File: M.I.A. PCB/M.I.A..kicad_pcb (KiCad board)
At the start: 6 copper layers, 50.8 x 106.6 mm, 160 parts, among them J1 USB_C_Receptacle_USB2.0_16P, J10 Conn_01x03, J11 Conn_01x03, J12 Conn_Coaxial, J13 Screw_Terminal_01x02, J14 Screw_Terminal_01x02, J15 Screw_Terminal_01x02, J16 Screw_Terminal_01x02, J17 Screw_Terminal_01x02, J18 Screw_Terminal_01x02, J2 Conn_01x02_Pin, J3 Conn_01x03, J4 Conn_01x03, J5 Conn_01x03, J6 Conn_01x03, J7 MSD-4-A, J8 Conn_01x03, J9 Conn_01x03, Q1 AO3400A, Q2 AO3400A, Q3 AO3400A, Q4 AO3400A, SW1 SW_Push, SW2 SW_Push, U1 W25Q128JVS, U11 AMS1117-3.3, U11 INA219AxDCN, U12 AP62150WU, U13 TPS2121RUXR, U14 AP62150WU, U15 74AHC541, U16 RFM95W-915S2, U17 TLV70233_SOT23-5, U2 RP2350B-QFN80, U3 MMC5983MA, U4 ICM-45686, U5 MS5611-01BA, U6 TMP117xxDRV, U7 MAX-M10S, U8 KX134-1211, U9 TPS2121RUXR, Y1 ABM8-272-T3

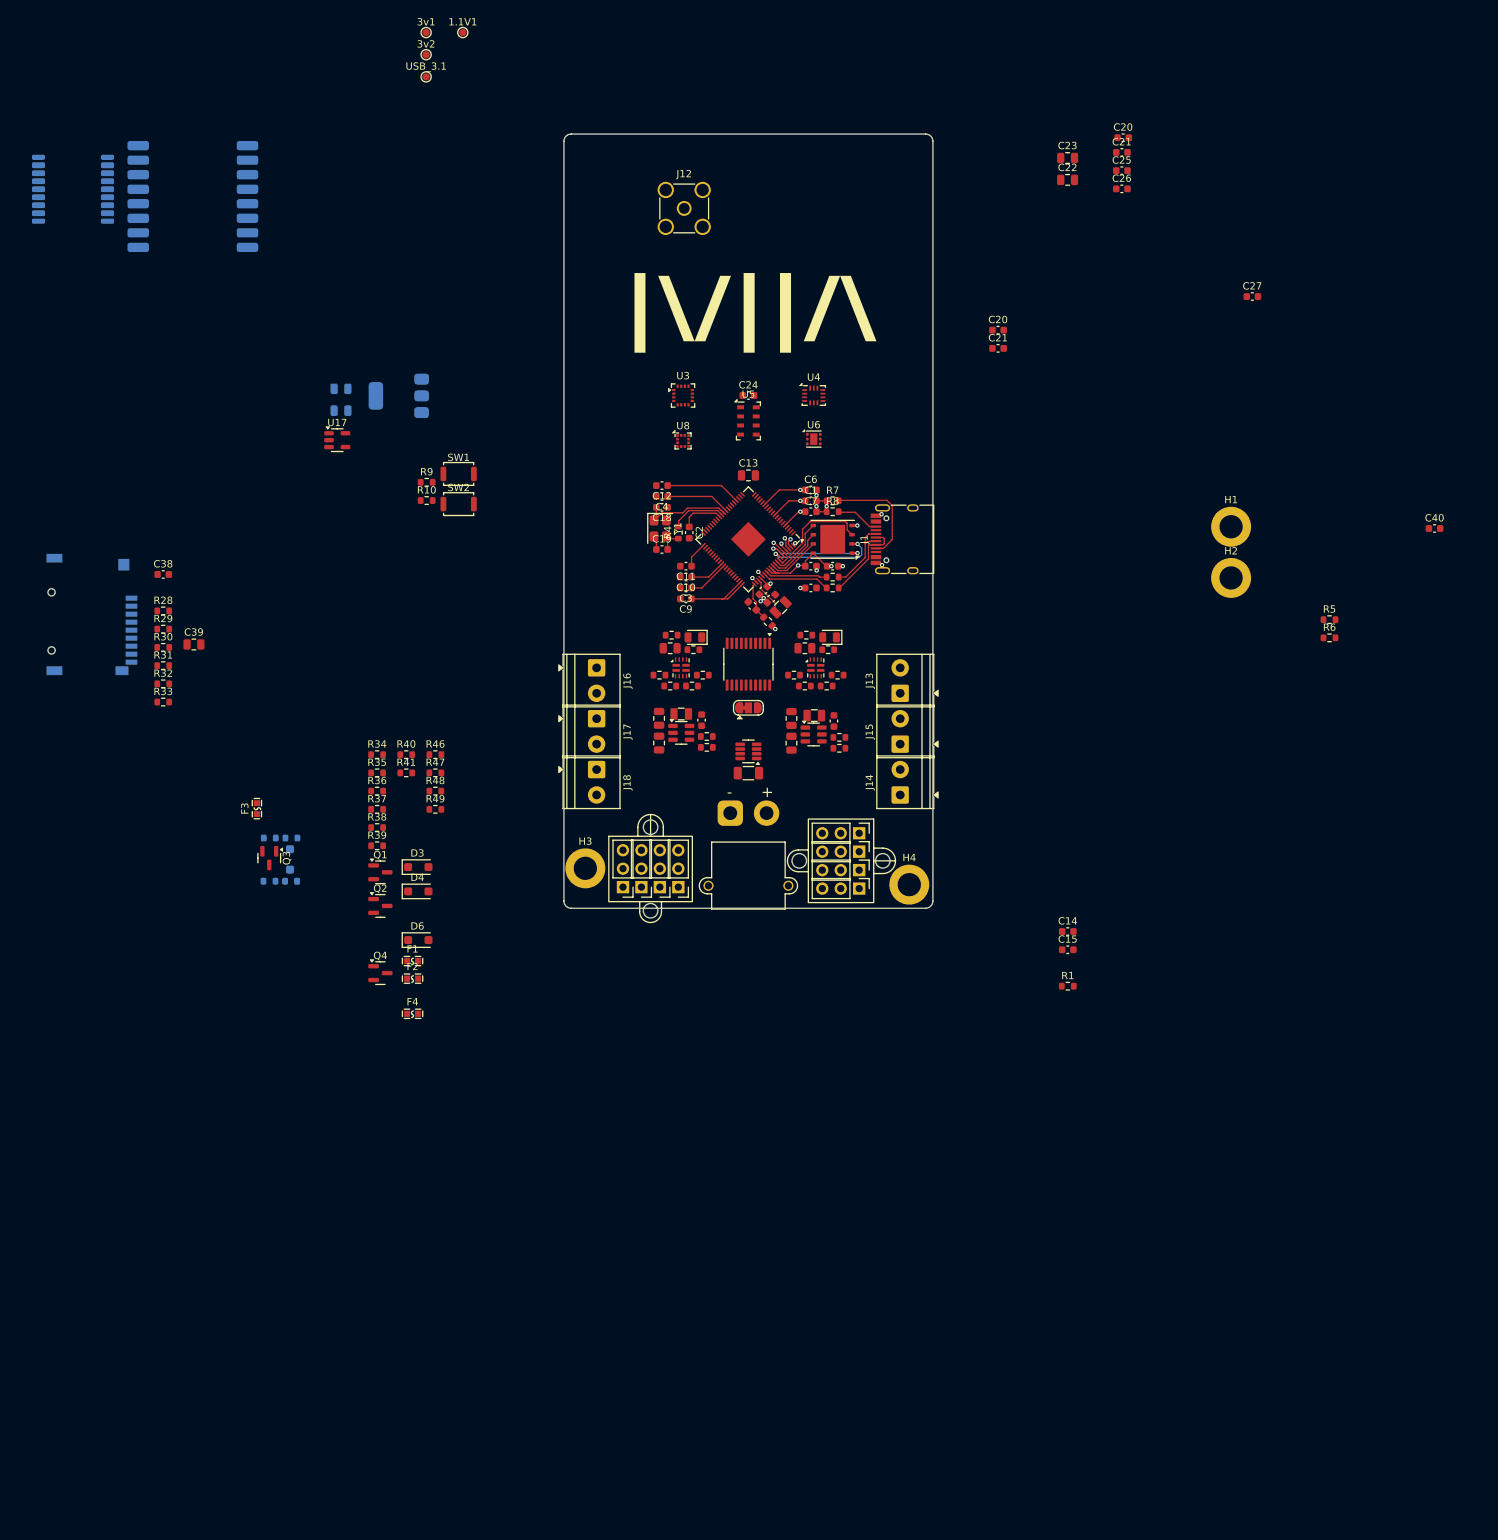
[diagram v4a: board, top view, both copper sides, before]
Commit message: Finished Layout other than gps, extra connectors, and ignition lines
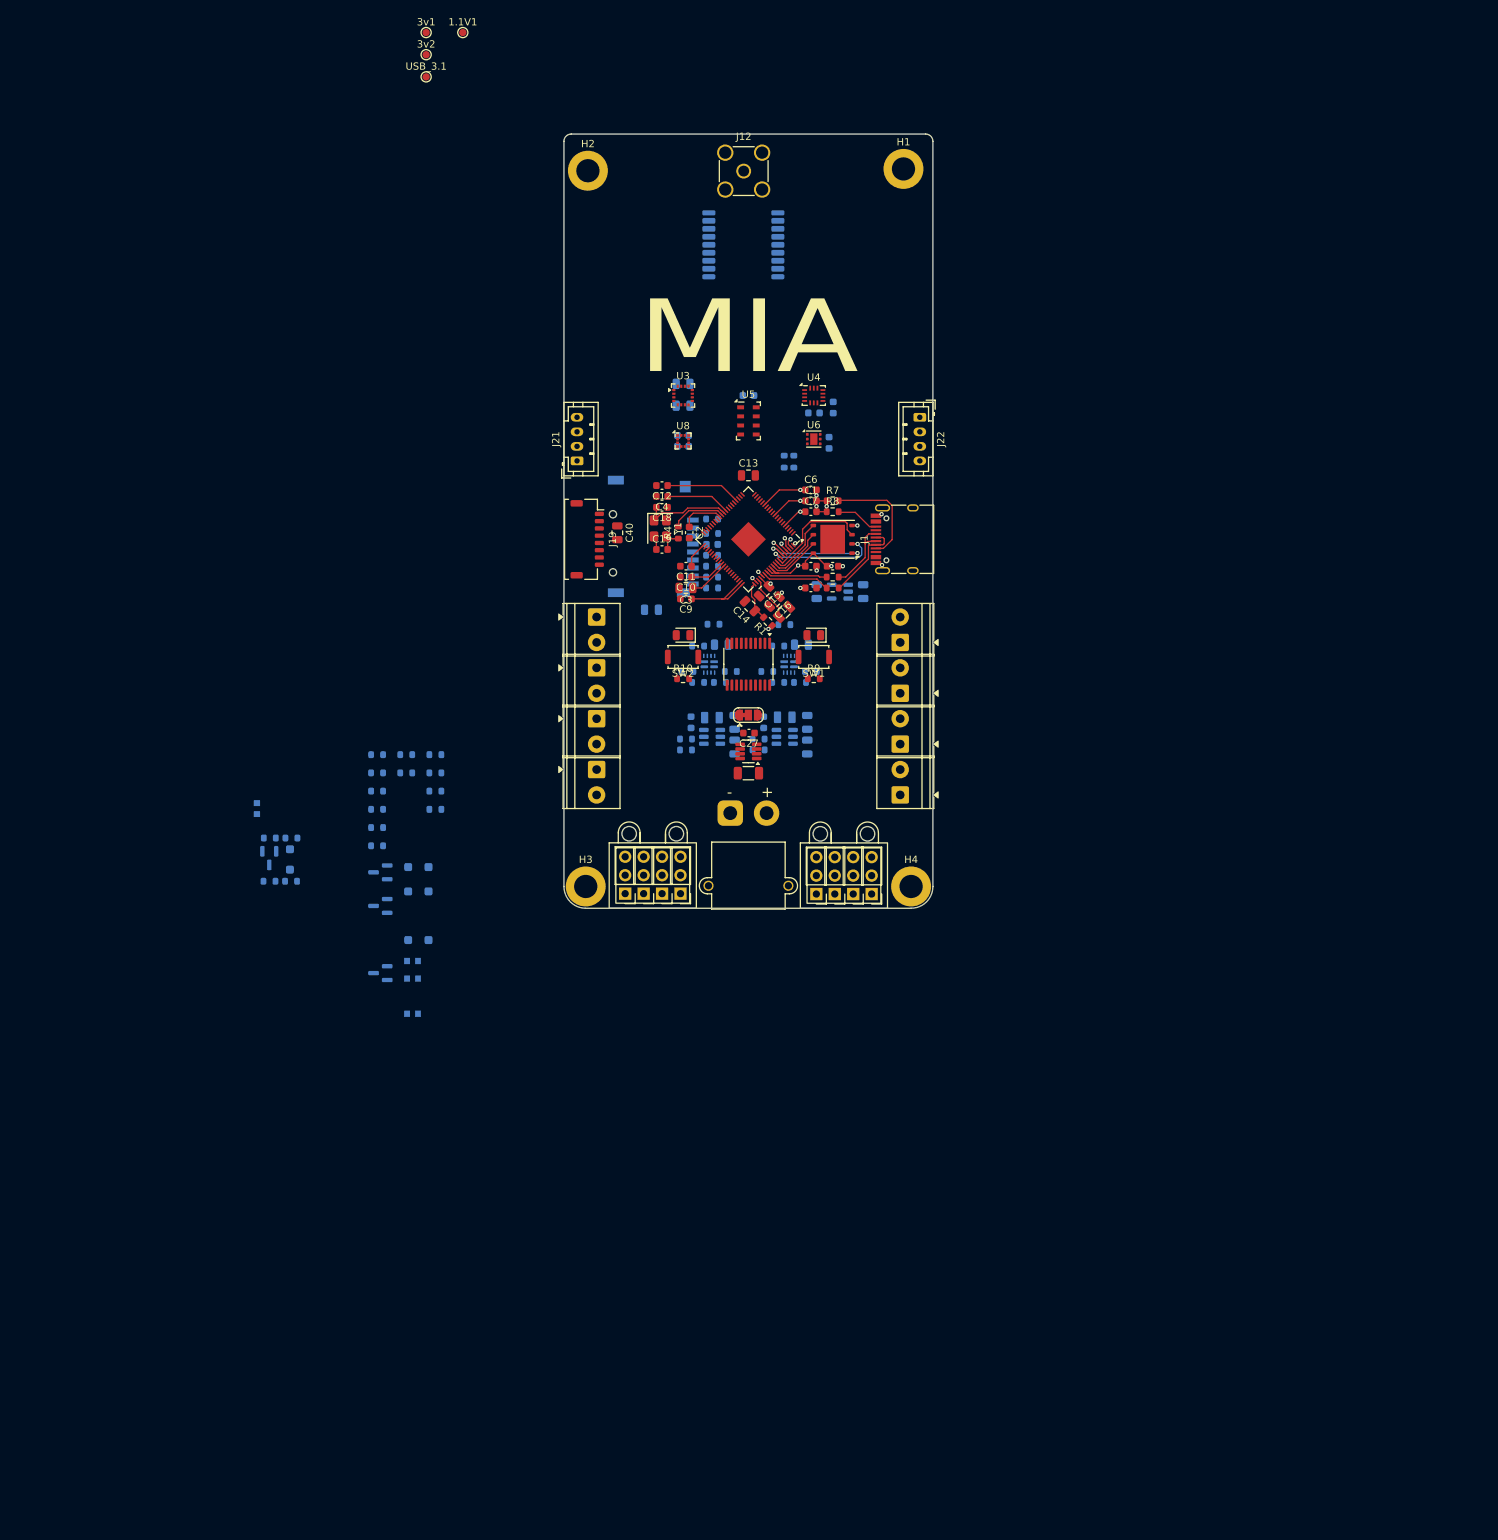
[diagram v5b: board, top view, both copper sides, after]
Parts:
- removed the C14 at (89.4, 124.8)
- removed the C14 at (45.9, 80.0)
- removed the C15 at (89.4, 127.3)
- removed the C15 at (47.5, 77.8)
- removed the C20 at (79.8, 42.0)
- removed the C20 at (97.0, 15.5)
- removed the C21 at (79.8, 44.5)
- removed the C21 at (96.8, 17.5)
- removed the R1 at (89.4, 132.3)
- removed the U11 at (-2.75, 51.0)
- removed U16: RFM95W-915S2, RF_Module:HOPERF_RFM9XW_SMD
- removed U17: TLV70233_SOT23-5, Package_TO_SOT_SMD:SOT-23-5
- added C14: 4.7u, Capacitor_SMD:C_0805_2012Metric, F.Cu at (45.6, 80.0)
- added C15: 4.7u, Capacitor_SMD:C_0805_2012Metric, F.Cu at (47.5, 78.0)
- added C20: 100n, Capacitor_SMD:C_0603_1608Metric, B.Cu at (54.4, 53.4)
- added C21: 100n, Capacitor_SMD:C_0603_1608Metric, B.Cu at (57.1, 52.6)
- added C41: 100n, Capacitor_SMD:C_0603_1608Metric, B.Cu at (56.5, 57.5)
- added J12: Screw_Terminal_01x02, TerminalBlock_Phoenix:TerminalBlock_Phoenix_PT-1,5-2-3.5-H_1x02_P3.50mm_Horizontal, F.Cu at (24.5, 81.5)
- added J19: Conn_01x08_Socket, Connector_JST:JST_SHL_SM08B-SHLS-TF_1x08-1MP_P1.00mm_Horizontal, F.Cu at (23.2, 70.8)
- added J20: Screw_Terminal_01x02, TerminalBlock_Phoenix:TerminalBlock_Phoenix_PT-1,5-2-3.5-H_1x02_P3.50mm_Horizontal, F.Cu at (66.3, 85.0)
- added J21: Conn_01x04_Socket, Connector_JST:JST_PH_B4B-PH-K_1x04_P2.00mm_Vertical, F.Cu at (21.8, 60.0)
- added J22: Conn_01x04_Socket, Connector_JST:JST_PH_B4B-PH-K_1x04_P2.00mm_Vertical, F.Cu at (69.0, 54.0)
- added U10: AP2112K-3.3, Package_TO_SOT_SMD:SOT-23-5, B.Cu at (58.0, 78.0)
- C16, C3: footprint Capacitor_SMD:C_0603_1608Metric -> Capacitor_SMD:C_0805_2012Metric
- C22, C23, C24, C25, C26, C28, C31, C32, C33, C34, C35, C36, C37, C38, C39, D3, D4, D6, F1, F2, F3, F4, L2, L3, Q1, Q2, Q3, Q4, R11, R12, R13, R14, R15, R17, R18, R19, R20, R21, R22, R23, R24, R25, R26, R27, R28, R29, R30, R31, R32, R33, R34, R35, R36, R37, R38, R39, R40, R41, R46, R47, R48, R49, R5, R6, U12, U13, U14, U9: moved to B.Cu
- C40: value 100n -> 10u; footprint Capacitor_SMD:C_0603_1608Metric -> Capacitor_SMD:C_0805_2012Metric
- moved C40 112.5 mm to (27.4, 69.9), turned to -90 degrees
- moved H2 104.8 mm to (23.3, 20.1)
- moved U7 92.6 mm to (44.7, 30.2)
- moved C27 91.7 mm to (45.5, 97.5), turned to 180 degrees
- moved R32 78.9 mm to (40.4, 68.0)
- moved R5 78.2 mm to (50.3, 60.1), turned to 90 degrees
- moved J7 78.0 mm to (30.0, 70.4)
- moved R6 77.7 mm to (51.6, 60.1), turned to 90 degrees
- moved R33 77.2 mm to (40.4, 77.5), turned to 180 degrees
- moved C29 77.1 mm to (61.2, 78.0), turned to -90 degrees
- moved R29 76.7 mm to (40.4, 70.0), turned to 180 degrees
- moved R30 76.6 mm to (40.4, 73.0), turned to 180 degrees
- moved R31 76.6 mm to (40.4, 76.0), turned to 180 degrees
- moved R28 75.8 mm to (40.4, 74.5), turned to 180 degrees
- moved C38 75.7 mm to (40.4, 71.5)
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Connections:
- U4 pad 5: Net-(U4-VDDIO) -> +3.3V
- U4 pad 8: Net-(U4-VDD) -> +3.3V
- U6 pad 1: unconnected-(U6-SCL-Pad1) -> SCL
- U6 pad 2: unconnected-(U6-GND-Pad2) -> GND
- U6 pad 4: unconnected-(U6-ADD0-Pad4) -> GND
- U6 pad 5: unconnected-(U6-V+-Pad5) -> +3.3V
- U6 pad 6: unconnected-(U6-SDA-Pad6) -> SDA
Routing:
- net +1V1: track 17.6 -> 23.0 mm, vias 2 -> 3
- net Net-(U2-VREG_LX): track 5.39 -> 6.25 mm
- net +3.3V: track 66.5 -> 67.2 mm
- net GND: vias 11 -> 9
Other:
- outline, holes or cut-outs redrawn
- board text added: "MIA"
- board text added: "SIG, GND, PWR(1.1/3v) PWR(5v,BATT,IGN) GND, SIG"
- board text removed: "|\/||/\"

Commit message: Worked More on Layout/Wiring
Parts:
- C38: moved to F.Cu
- J12, J13, J14, J15, J16, J17, J18, J20: footprint TerminalBlock_Phoenix:TerminalBlock_Phoenix_PT-1,5-2-3.5-H_1x02_P3.50mm_Horizontal -> PCM_SparkFun-Connector:ScrewTerminal_1x02_P3.5mm_Horizontal_Black
- moved R28 47.8 mm to (-6.53, 65.3)
- moved R31 47.8 mm to (-6.53, 66.8), turned to 0 degrees
- moved R33 47.8 mm to (-6.53, 68.3)
- moved R30 41.8 mm to (-1.10, 67.8), turned to -90 degrees
- moved R29 40.0 mm to (0.42, 67.8), turned to -90 degrees
- moved C39 38.6 mm to (-5.85, 73.2)
- moved R32 38.5 mm to (1.93, 67.8), turned to 90 degrees
- moved R43 9.80 mm to (-13.9, 102.8)
- moved R44 9.80 mm to (-16.9, 102.8)
- moved D5 9.80 mm to (-14.2, 105.8)
- moved F3 9.80 mm to (-18.7, 98.8)
- moved Q3 9.80 mm to (-17.0, 105.6)
- moved R42 9.80 mm to (-17.0, 108.8)
- moved R45 9.80 mm to (-14.0, 108.8)
- moved C38 7.24 mm to (33.5, 73.7), turned to 180 degrees
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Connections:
- U2 pad 39: unconnected-(U2-GPIO31-Pad39) -> IGN_4
- U2 pad 40: unconnected-(U2-GPIO32-Pad40) -> IGN_3
- U2 pad 42: unconnected-(U2-GPIO33-Pad42) -> IGN_2
- U2 pad 43: unconnected-(U2-GPIO34-Pad43) -> IGN_1
- U2 pad 44: unconnected-(U2-GPIO35-Pad44) -> SD_ChipDetect
- U2 pad 45: unconnected-(U2-GPIO36-Pad45) -> SPI_MISO_SD
- U2 pad 46: unconnected-(U2-GPIO37-Pad46) -> SD_ChipSelect
- U2 pad 47: unconnected-(U2-GPIO38-Pad47) -> SPI_SCK_SD
- U2 pad 48: unconnected-(U2-GPIO39-Pad48) -> SPI_MOSI_SD
- U2 pad 49: unconnected-(U2-GPIO40_ADC0-Pad49) -> PWM8
- U2 pad 52: unconnected-(U2-GPIO41_ADC1-Pad52) -> PWM7
- U2 pad 53: unconnected-(U2-GPIO42_ADC2-Pad53) -> PWM6
- U2 pad 54: unconnected-(U2-GPIO43_ADC3-Pad54) -> PWM5
- U2 pad 55: unconnected-(U2-GPIO44_ADC4-Pad55) -> PWM4
- U2 pad 56: unconnected-(U2-GPIO45_ADC5-Pad56) -> PWM3
- U2 pad 57: unconnected-(U2-GPIO46_ADC6-Pad57) -> PWM1
- U2 pad 58: unconnected-(U2-GPIO47_ADC7-Pad58) -> PWM2
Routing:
- net GND: track 12.8 -> 55.0 mm, vias 9 -> 41
- net /Peripherals/servo1: track 0.00 -> 36.1 mm
- net /Peripherals/servo2: track 0.00 -> 35.3 mm
- net /Peripherals/servo4: track 0.00 -> 34.6 mm
- net /Peripherals/servo8: track 0.00 -> 34.5 mm
- net /Peripherals/servo3: track 0.00 -> 34.5 mm
- net /Peripherals/servo7: track 0.00 -> 33.7 mm
- net /Peripherals/servo6: track 0.00 -> 33.6 mm
- net /Peripherals/servo5: track 0.00 -> 32.2 mm
- net PWM7: track 0.00 -> 16.9 mm, vias 0 -> 2
- net PWM8: track 0.00 -> 14.8 mm, vias 0 -> 2
- net PWM6: track 0.00 -> 14.1 mm, vias 0 -> 2
- net +3.3V: track 67.2 -> 81.2 mm, vias 8 -> 20
- net PWM5: track 0.00 -> 13.7 mm, vias 0 -> 2
- net PWM1: track 0.00 -> 13.2 mm
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- added copper zone on F.Cu, net +1V1
- added copper zone on In2.Cu, net +1V1
- added copper zone on B.Cu, net +5V_USB
- added copper zone on B.Cu, net 5v_Batt
- added copper zone on B.Cu, net GND
- added copper zone on In4.Cu, net GND
- added copper zone on B.Cu, net Net-(U12-FB)
- added copper zone on B.Cu, net Net-(U14-FB)
- added copper zone on F.Cu, net VBAT
- added copper zone on B.Cu, net VSYS
- added copper zone on F.Cu, net VSYS
- added copper zone on In3.Cu, net VSYS
- added copper zone on In3.Cu, net V_IGN
